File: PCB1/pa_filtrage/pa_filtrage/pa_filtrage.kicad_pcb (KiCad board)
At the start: 2 copper layers, 17 parts, among them J1 Conn_Coaxial, J2 Conn_Coaxial, J4 Conn_01x02_Pin, U1 SKY66185-11

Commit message: PCB1 fini à valider
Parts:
- added J3: Conn_01x02_Pin, Connector_PinHeader_2.54mm:PinHeader_1x02_P2.54mm_Vertical, F.Cu at (1.79, 1.79)
- moved J1 6.22 mm to (174.8, 64.9)
- moved J3 4.74 mm to (190.3, 56.1)
- moved C7 4.37 mm to (181.9, 64.9)
- moved C4 4.20 mm to (188.7, 61.2)
- moved C5 4.20 mm to (188.7, 59.6)
- moved C1 4.19 mm to (184.6, 61.1)
- moved C2 4.19 mm to (184.6, 59.5)
- moved U1 4.14 mm to (186.9, 64.9)
- moved L2 4.14 mm to (191.4, 64.4)
- moved L3 4.08 mm to (198.3, 64.4)
- moved C10 4.03 mm to (190.7, 66.8)
- moved C11 3.98 mm to (199.0, 67.0)
- moved SF1 3.91 mm to (193.3, 62.8)
- moved J2 3.79 mm to (203.3, 64.5)
- moved R1 3.77 mm to (183.2, 67.8)
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- renumbered J4 to J3
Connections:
- net 3.3V renamed +3.3V
- U1 pad 29: EXP_25 -> EXP_7
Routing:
- net +3.3V: track 0.00 -> 40.8 mm, vias 0 -> 1
- net RFIN: track 0.00 -> 6.35 mm
- net FiltreOUT: track 0.00 -> 6.17 mm
- net FiltreIN: track 0.00 -> 3.01 mm
- net Net-(U1-RFIN): track 0.00 -> 1.85 mm
- net Net-(U1-~{VEN}): track 0.00 -> 1.60 mm
- net Net-(SF1-IN): track 0.00 -> 1.48 mm
- net Net-(SF1-OUT): track 0.00 -> 1.45 mm
- net GND: vias 0 -> 1
- added copper zone on B.Cu, net GND
- added copper zone on F.Cu, net GND
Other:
- board outline added: 34.7 x 21.3 mm

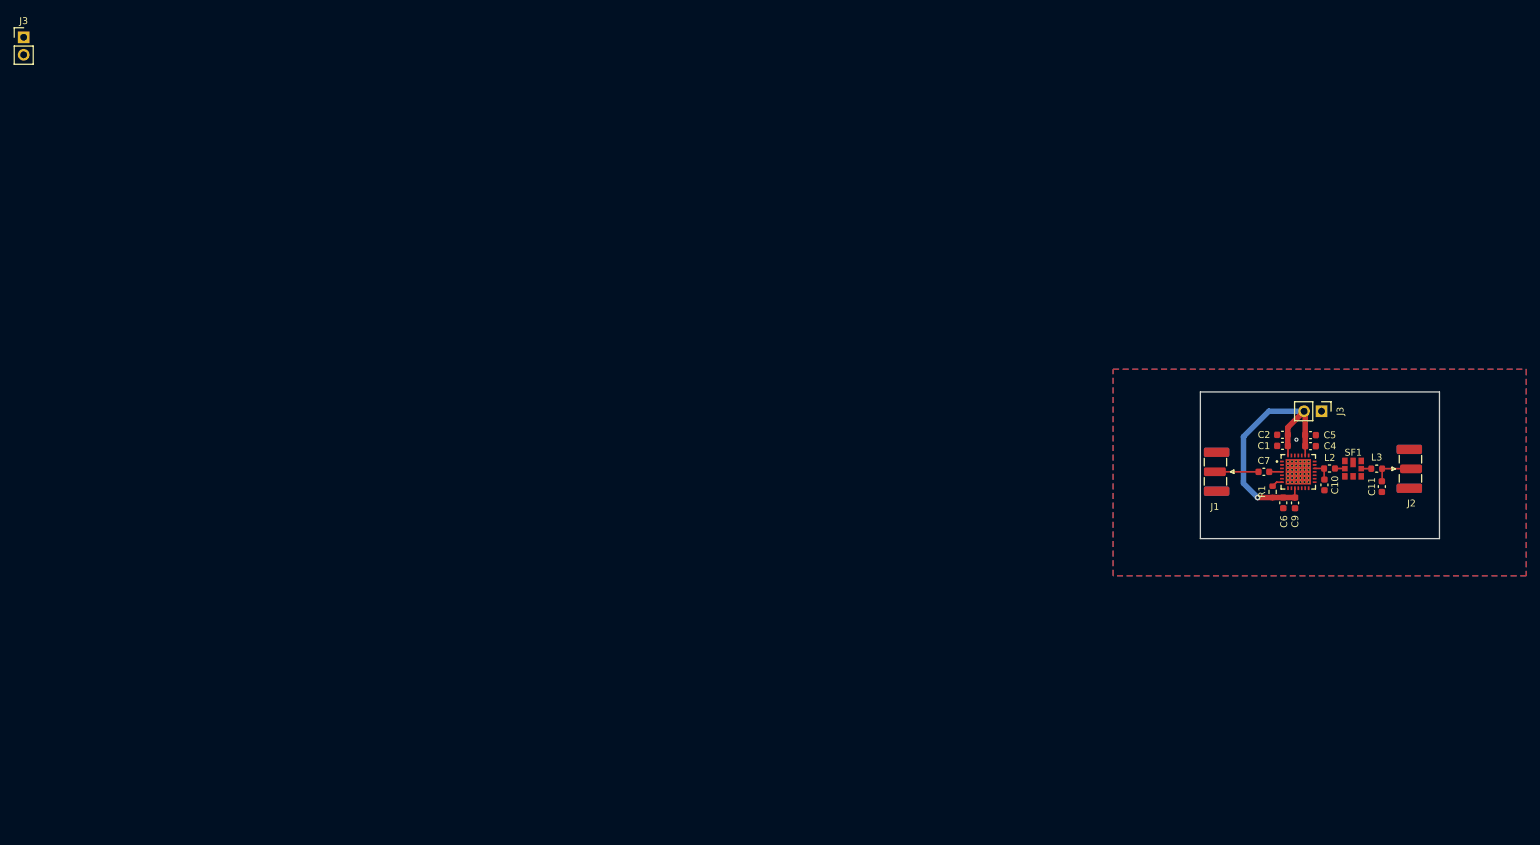
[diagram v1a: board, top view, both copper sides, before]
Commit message: Correction footprints SKY à jour
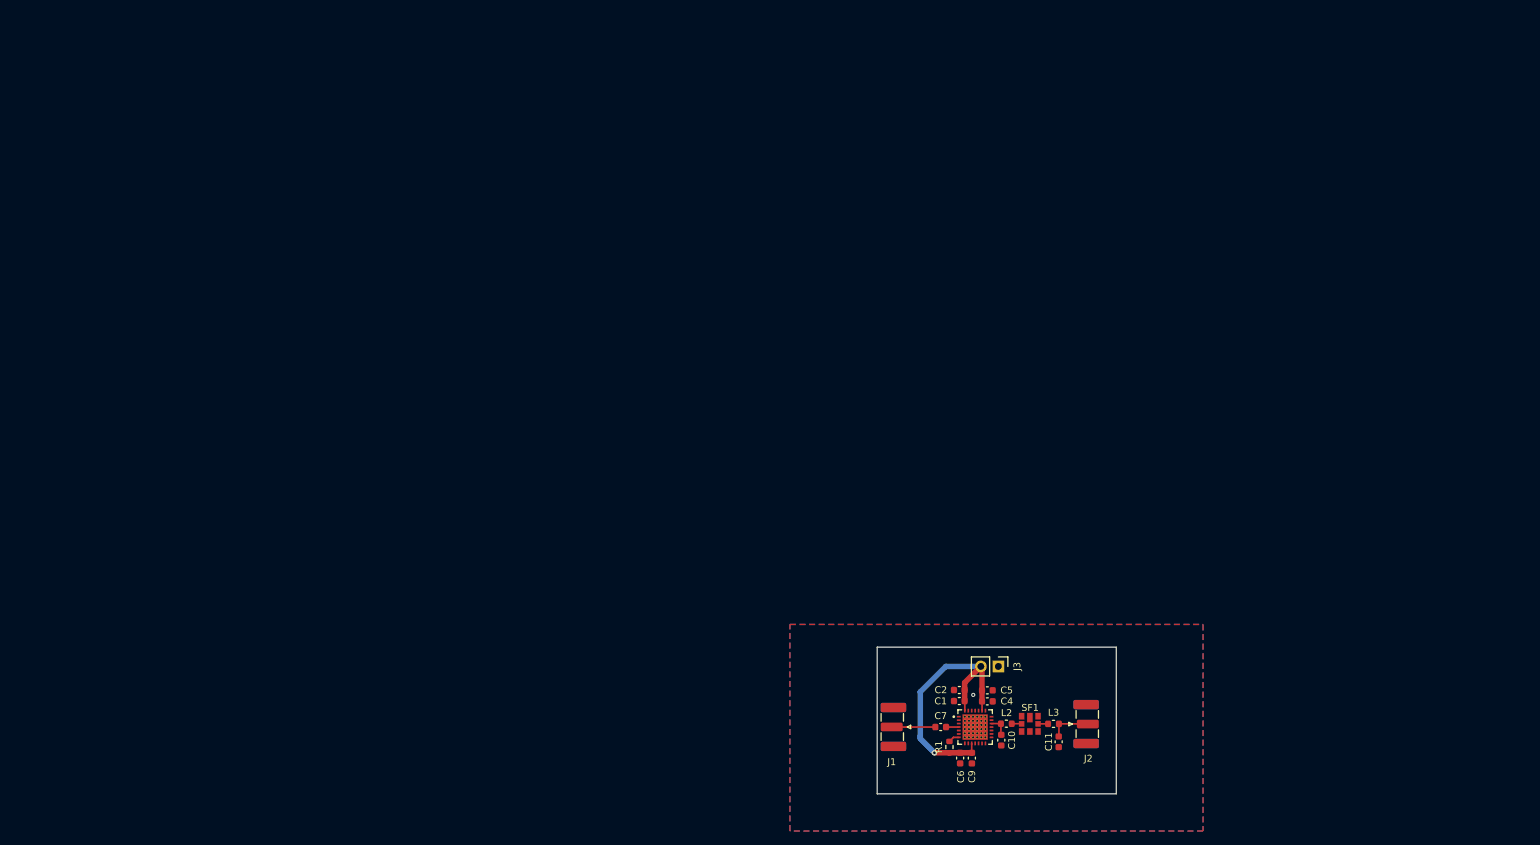
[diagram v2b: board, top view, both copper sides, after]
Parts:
- removed the J3 at (1.79, 1.79)
- moved C1 59.8 mm to (137.7, 98.2)
- moved C10 59.8 mm to (143.8, 103.9)
- moved C11 59.8 mm to (152.1, 104.1)
- moved C4 59.8 mm to (141.7, 98.2)
- moved C9 59.8 mm to (139.5, 106.5)
- moved J1 59.8 mm to (127.9, 102.0)
- moved J2 59.8 mm to (156.3, 101.5)
- moved L3 59.8 mm to (151.3, 101.5)
- moved R1 59.8 mm to (136.2, 104.9)
- moved SF1 59.8 mm to (146.3, 99.9)
- moved C2 59.8 mm to (137.7, 96.6)
- moved C5 59.8 mm to (141.7, 96.6)
- moved C6 59.8 mm to (137.8, 106.5)
- moved C7 59.8 mm to (135.0, 102.0)
- moved J3 59.8 mm to (143.3, 93.2)
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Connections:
- net EXP_7 renamed EXP_9

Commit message: Updated edge cut
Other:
- board size 34.7 x 21.3 mm -> 32.7 x 21.3 mm
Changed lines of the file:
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@@
 	(gr_rect
 		(start 125.7465 90.363)
-		(end 160.4685 111.663)
+		(end 158.4455 111.663)
 		(stroke
 			(width 0.05)
